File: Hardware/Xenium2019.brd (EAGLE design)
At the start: 39.4 x 36.2 mm, 20 parts, among them J1 SM10B-SRSS-TB, Q1 310mA/60V/1.6Ω, Q2 310mA/60V/1.6Ω, Q3 310mA/60V/1.6Ω, Q4 310mA/60V/1.6Ω, U1 XC9572XL-10VQG64, U2 AM29LV160M

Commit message: Update: added pads
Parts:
- J1: value SM10B-SRSS-TB -> (none); device my-library:SM10B-SRSS-TB -> con-lsta:FE10
- moved J1 13.7 mm to (10.2, -7.62)
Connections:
- net GND: no longer J1.C1, J1.C2
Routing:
- net GND: track 37.6 -> 29.0 mm, vias 18 -> 15
- net CS: track 6.50 -> 4.84 mm
- net B_EXT: track 19.2 -> 17.8 mm
- net MOSI: track 13.8 -> 12.4 mm
- net SCK: track 10.2 -> 8.80 mm
- net G_EXT: track 23.4 -> 22.0 mm
- net MISO: track 15.4 -> 14.1 mm
- net INPUT: track 6.20 -> 4.91 mm

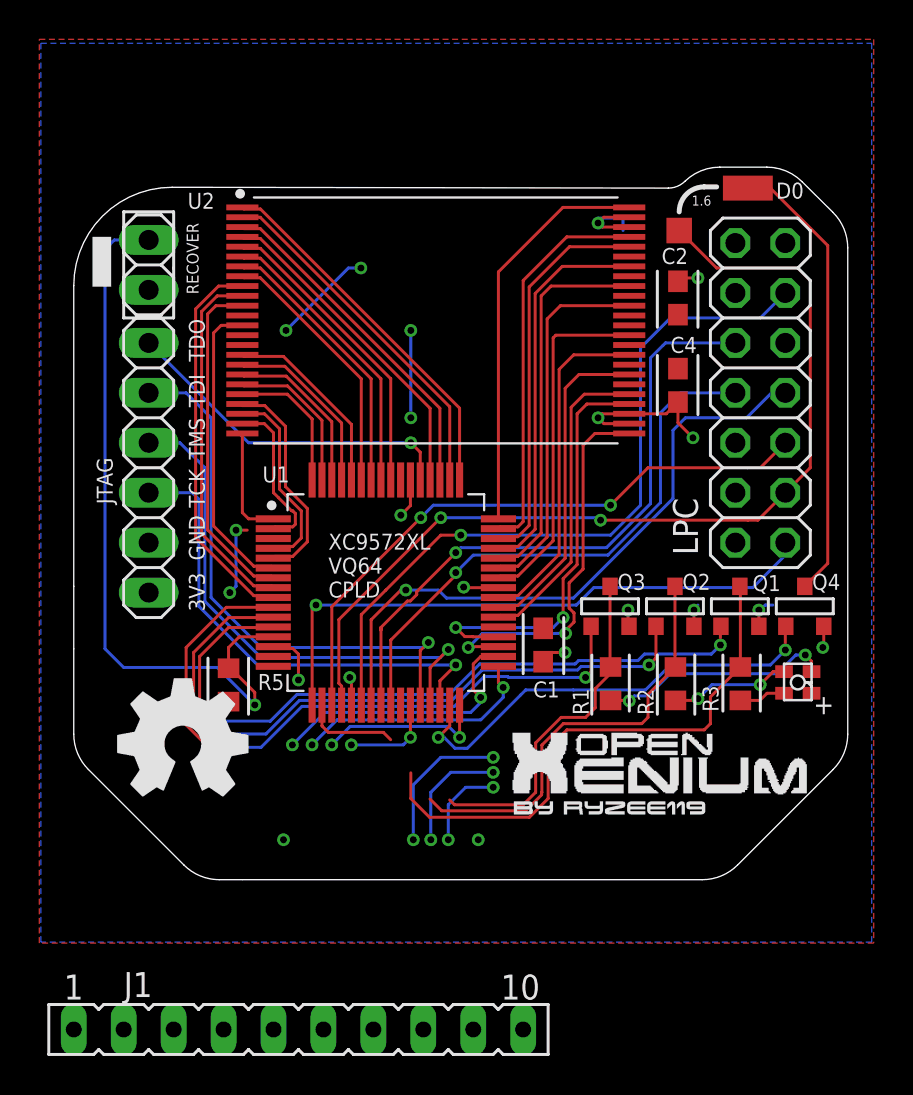
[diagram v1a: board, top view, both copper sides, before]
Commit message: Update: wired header
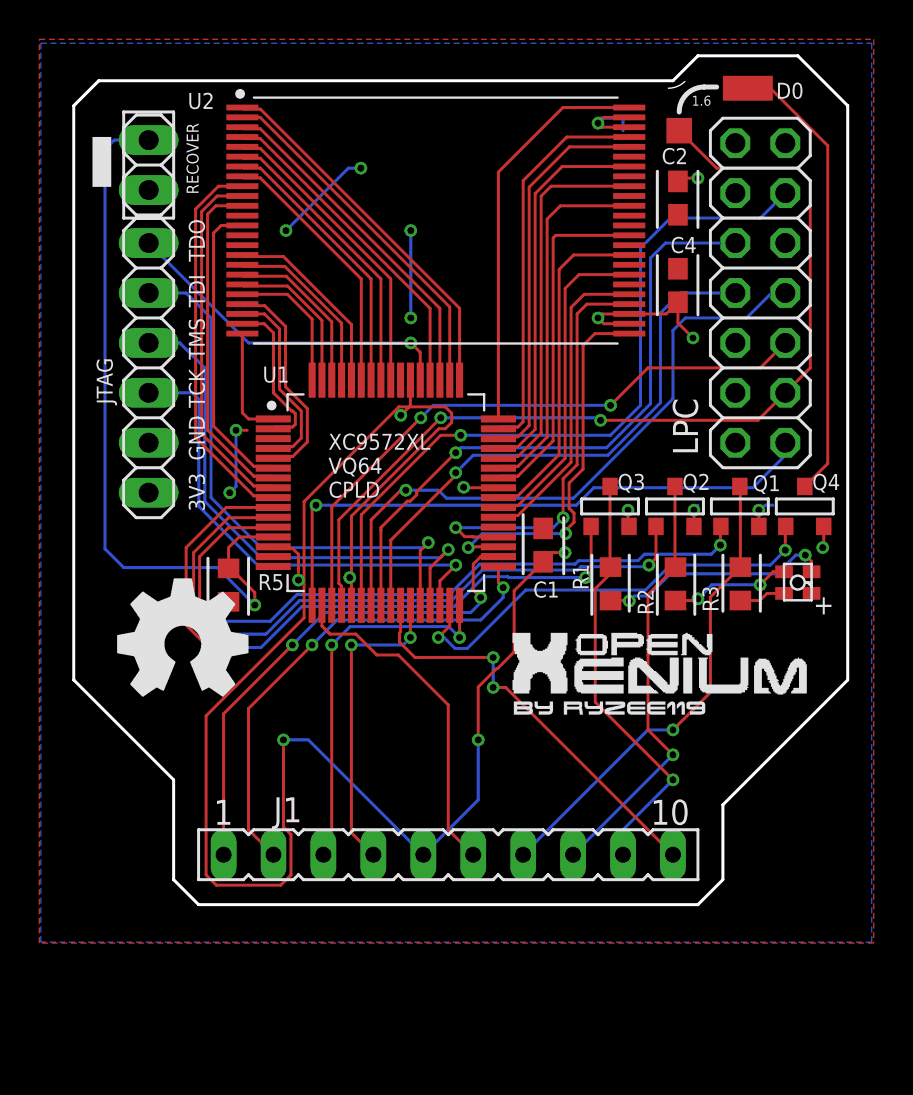
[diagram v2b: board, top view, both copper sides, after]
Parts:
- moved J1 11.7 mm to (17.8, 1.27)
- moved JTAG 5.08 mm to (2.54, 26.0)
- moved C1 5.08 mm to (22.6, 17.0)
- moved L1 5.08 mm to (35.6, 15.1)
- moved Q1 5.08 mm to (32.6, 19.0)
- moved Q2 5.08 mm to (29.3, 19.0)
- moved Q3 5.08 mm to (26.0, 19.0)
- moved Q4 5.08 mm to (35.9, 19.0)
- moved R1 5.08 mm to (26.0, 15.0)
- moved R2 5.08 mm to (29.3, 15.0)
- moved R3 5.08 mm to (32.6, 15.0)
- moved R5 5.08 mm to (6.60, 15.0)
- moved C2 5.08 mm to (29.5, 34.7)
- moved C4 5.08 mm to (29.5, 30.2)
- moved D0 5.08 mm to (33.0, 40.3)
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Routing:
- net GND: track 29.0 -> 110.5 mm
- net MOSI: track 12.4 -> 24.9 mm
- net CS: track 4.84 -> 17.3 mm
- net MISO: track 14.1 -> 26.2 mm
- net INPUT: track 4.91 -> 16.0 mm
- net SCK: track 8.80 -> 19.6 mm
- net +3V3: track 31.3 -> 35.9 mm, vias 12 -> 8
- net B_EXT: track 17.8 -> 21.7 mm, vias 0 -> 1
- net R_EXT: track 28.0 -> 24.1 mm, vias 0 -> 1
- net G_EXT: vias 0 -> 1
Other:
- board size 39.4 x 36.2 mm -> 39.4 x 43.2 mm
